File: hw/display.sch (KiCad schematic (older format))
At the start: 3 parts, among them J6 IDC_02X03, SW1 LCD_BTN

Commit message: updated schematic added footptints
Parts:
- C26: footprint (none) -> Capacitor_SMD:C_0805_2012Metric
- SW1: footprint (none) -> Button_Switch_SMD:SW_SPST_FSMSM
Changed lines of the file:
@@
 F 0 "SW1" V 2604 2848 50  0000 L CNN
 F 1 "LCD_BTN" V 2695 2848 50  0000 L CNN
-F 2 "" H 2650 2900 50  0001 C CNN
+F 2 "Button_Switch_SMD:SW_SPST_FSMSM" H 2650 2900 50  0001 C CNN
 F 3 "" H 2650 2900 50  0001 C CNN
 	1    2650 2700
@@
 F 0 "C26" H 2365 2746 50  0000 L CNN
 F 1 "100n" H 2365 2655 50  0000 L CNN
-F 2 "" H 2288 2550 50  0001 C CNN
+F 2 "Capacitor_SMD:C_0805_2012Metric" H 2288 2550 50  0001 C CNN
 F 3 "~" H 2250 2700 50  0001 C CNN
 	1    2250 2700

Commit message: updated schematic
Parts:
- J6: footprint Connectors:IDC_Header_Straight_6pins -> Connector_IDC:IDC-Header_2x03_P2.54mm_Vertical
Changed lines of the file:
@@
 F 0 "J6" H 5000 3092 50  0000 C CNN
 F 1 "IDC_02X03" H 5000 3001 50  0000 C CNN
-F 2 "Connectors:IDC_Header_Straight_6pins" V 5550 2750 50  0001 C CNN
+F 2 "Connector_IDC:IDC-Header_2x03_P2.54mm_Vertical" V 5550 2750 50  0001 C CNN
 F 3 "~" V 5500 2750 50  0001 C CNN
 	1    5000 2750

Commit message: removed LCD RST signal
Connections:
- net ~LCD_RST is gone; now on net +3V3: J6.2
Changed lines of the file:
@@
 Text Label 4300 2750 0    50   ~ 0
 LCD_TX
-Text Label 5700 2650 2    50   ~ 0
-~RST
 Text HLabel 4200 2750 0    50   Output ~ 0
 LCD_UART_TX
 Text HLabel 5800 2750 2    50   Input ~ 0
 LCD_UART_RX
-Text HLabel 5800 2650 2    50   Input ~ 0
-~LCD_RST
-Wire Wire Line
-	5300 2650 5800 2650
 Wire Wire Line
 	5300 2750 5800 2750
@@
 Wire Wire Line
 	1750 2450 2250 2450
+$Comp
+L KLIB_Power:+3V3 #PWR?
+U 1 1 5ADC0B6F
+P 5350 2600
+F 0 "#PWR?" H 5350 2300 50  0001 C CNN
+F 1 "+3V3" H 5355 2773 50  0000 C CNN
+F 2 "" H 5350 2600 50  0001 C CNN
+F 3 "" H 5350 2600 50  0001 C CNN
+	1    5350 2600
+	1    0    0    -1
+$EndComp
+Wire Wire Line
+	5300 2650 5350 2650
+Wire Wire Line
+	5350 2650 5350 2600
 $EndSCHEMATC

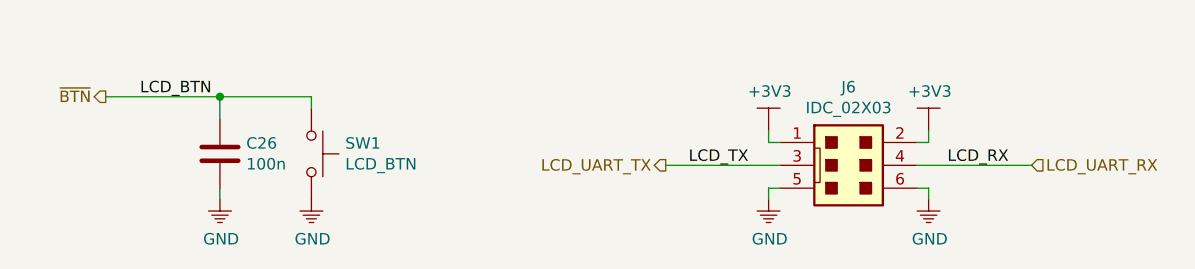
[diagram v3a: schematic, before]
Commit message: updated button RC filter
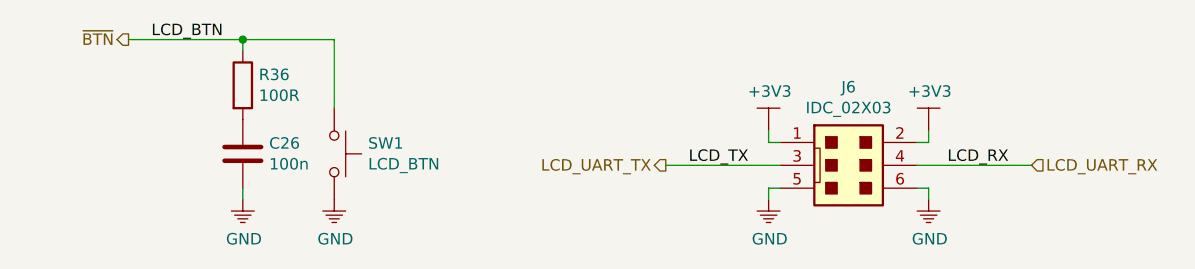
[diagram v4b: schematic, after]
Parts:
- added R36: 100R, Resistor_SMD:R_0805_2012Metric, symbol Device:R
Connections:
- net ~BTN: now also R36.1; no longer C26.1
- new net: C26.1, R36.2
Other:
- moved on the sheet: C26, SW1
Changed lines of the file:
@@
 L Switch:SW_Push SW1
 U 1 1 5ACFBDC5
-P 2650 2700
-F 0 "SW1" V 2604 2848 50  0000 L CNN
-F 1 "LCD_BTN" V 2695 2848 50  0000 L CNN
-F 2 "Button_Switch_SMD:SW_SPST_FSMSM" H 2650 2900 50  0001 C CNN
-F 3 "" H 2650 2900 50  0001 C CNN
-	1    2650 2700
+P 2750 2700
+F 0 "SW1" V 2704 2848 50  0000 L CNN
+F 1 "LCD_BTN" V 2795 2848 50  0000 L CNN
+F 2 "Button_Switch_SMD:SW_SPST_FSMSM" H 2750 2900 50  0001 C CNN
+F 3 "" H 2750 2900 50  0001 C CNN
+	1    2750 2700
 	0    1    1    0
 $EndComp
@@
 L Device:C C26
 U 1 1 5ACFBDCC
-P 2250 2700
-F 0 "C26" H 2365 2746 50  0000 L CNN
-F 1 "100n" H 2365 2655 50  0000 L CNN
-F 2 "Capacitor_SMD:C_0805_2012Metric" H 2288 2550 50  0001 C CNN
-F 3 "~" H 2250 2700 50  0001 C CNN
-	1    2250 2700
+P 2350 2700
+F 0 "C26" H 2465 2746 50  0000 L CNN
+F 1 "100n" H 2465 2655 50  0000 L CNN
+F 2 "Capacitor_SMD:C_0805_2012Metric" H 2388 2550 50  0001 C CNN
+F 3 "~" H 2350 2700 50  0001 C CNN
+	1    2350 2700
 	1    0    0    -1
 $EndComp
@@
 L KLIB_Power:GND #PWR044
 U 1 1 5ACFBDD3
-P 2650 2900
-F 0 "#PWR044" H 2650 2700 50  0001 C CNN
-F 1 "GND" H 2655 2727 50  0000 C CNN
-F 2 "" H 2650 2900 50  0001 C CNN
-F 3 "" H 2650 2900 50  0001 C CNN
-	1    2650 2900
+P 2750 2900
+F 0 "#PWR044" H 2750 2700 50  0001 C CNN
+F 1 "GND" H 2755 2727 50  0000 C CNN
+F 2 "" H 2750 2900 50  0001 C CNN
+F 3 "" H 2750 2900 50  0001 C CNN
+	1    2750 2900
 	1    0    0    -1
 $EndComp
@@
 L KLIB_Power:GND #PWR043
 U 1 1 5ACFBDD9
-P 2250 2900
-F 0 "#PWR043" H 2250 2700 50  0001 C CNN
-F 1 "GND" H 2255 2727 50  0000 C CNN
-F 2 "" H 2250 2900 50  0001 C CNN
-F 3 "" H 2250 2900 50  0001 C CNN
-	1    2250 2900
+P 2350 2900
+F 0 "#PWR043" H 2350 2700 50  0001 C CNN
+F 1 "GND" H 2355 2727 50  0000 C CNN
+F 2 "" H 2350 2900 50  0001 C CNN
+F 3 "" H 2350 2900 50  0001 C CNN
+	1    2350 2900
 	1    0    0    -1
 $EndComp
 Wire Wire Line
-	2250 2900 2250 2850
+	2350 2900 2350 2850
 Wire Wire Line
-	2650 2500 2650 2450
-Wire Wire Line
-	2650 2450 2250 2450
-Wire Wire Line
-	2250 2550 2250 2450
-Connection ~ 2250 2450
-Text Label 1900 2450 0    50   ~ 0
+	2750 2500 2750 2200
+Text Label 1950 2200 0    50   ~ 0
 LCD_BTN
-Text HLabel 1750 2450 0    50   Output ~ 0
+Text HLabel 1850 2200 0    50   Output ~ 0
 ~BTN
-Wire Wire Line
-	1750 2450 2250 2450
 $Comp
-L KLIB_Power:+3V3 #PWR?
+L KLIB_Power:+3V3 #PWR0101
 U 1 1 5ADC0B6F
 P 5350 2600
-F 0 "#PWR?" H 5350 2300 50  0001 C CNN
+F 0 "#PWR0101" H 5350 2300 50  0001 C CNN
 F 1 "+3V3" H 5355 2773 50  0000 C CNN
 F 2 "" H 5350 2600 50  0001 C CNN
@@
 Wire Wire Line
 	5350 2650 5350 2600
+Wire Wire Line
+	1850 2200 2350 2200
+$Comp
+L Device:R R36
+U 1 1 5ADDA201
+P 2350 2400
+F 0 "R36" H 2420 2446 50  0000 L CNN
+F 1 "100R" H 2420 2355 50  0000 L CNN
+F 2 "Resistor_SMD:R_0805_2012Metric" V 2280 2400 50  0001 C CNN
+F 3 "~" H 2350 2400 50  0001 C CNN
+	1    2350 2400
+	1    0    0    -1
+$EndComp
+Wire Wire Line
+	2350 2250 2350 2200
+Connection ~ 2350 2200
+Wire Wire Line
+	2350 2200 2750 2200
 $EndSCHEMATC
